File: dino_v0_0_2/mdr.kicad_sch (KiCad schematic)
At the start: 12 parts, among them U18 74LS373, U22 74LS02, U25 74LS245, U34 74LS373, U37 74LS04, U39 74LS00

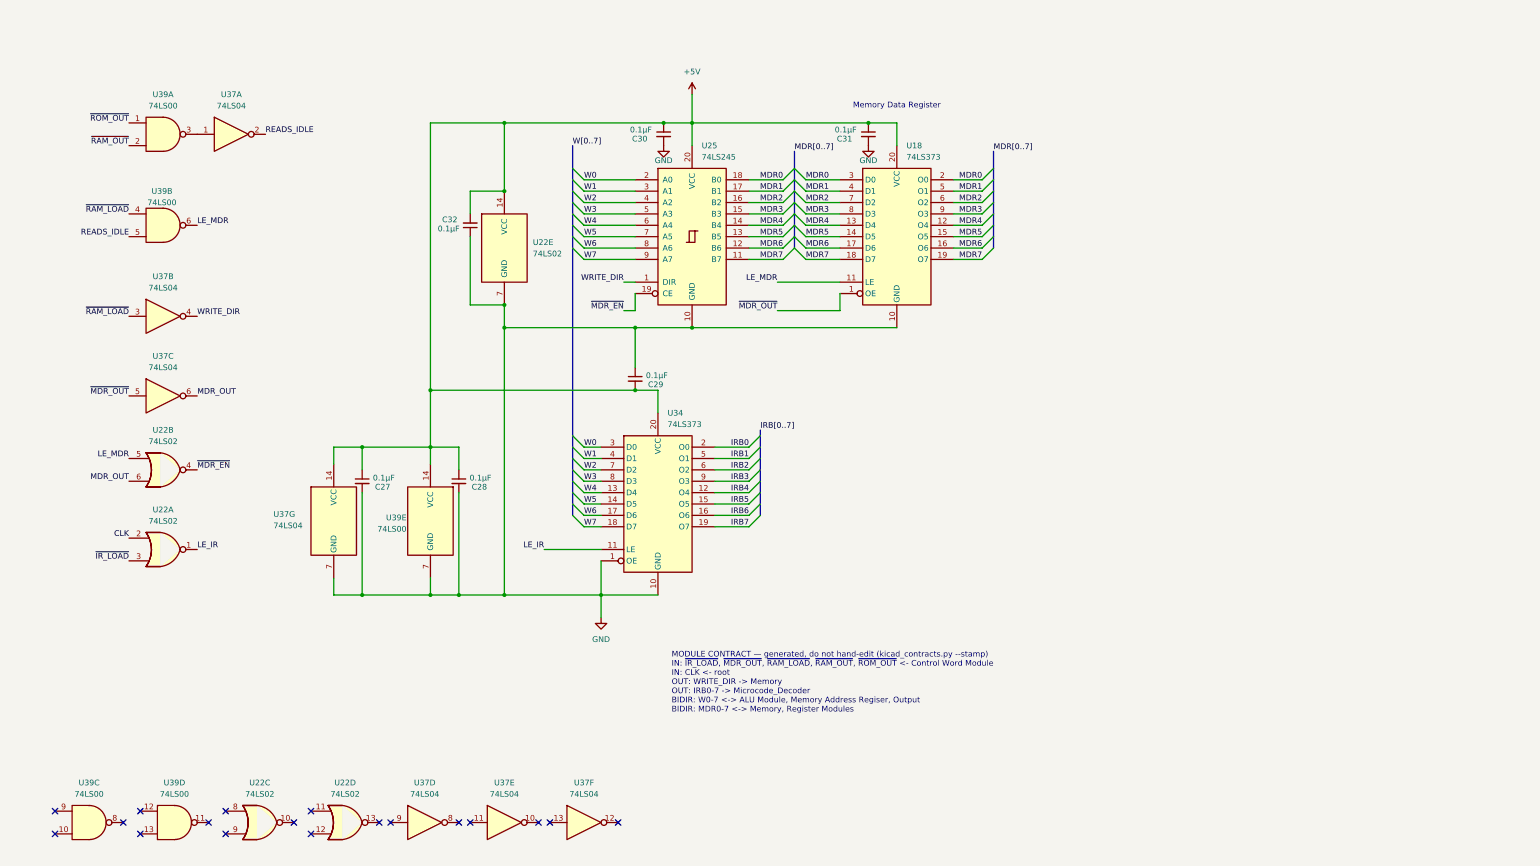
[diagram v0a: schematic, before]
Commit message: Machine Complete
All ten DINO modules bench-proven on the ATmega2560 rig: root, pc,
microcode, control_word, mdr, registers, mar, memory, alu, io. Coverage
lint reports 0 gaps and 0 pending.

Test modules (mod_*.c) plus host-tested expect models (cw/mdr/reg/mar/
mem/alu_expect.h) — pure logic, no AVR headers, exhaustive host tests
written RED before any bench run. Every assertion was netlist-verified
against the schematic before it was encoded.

Generators, so no table is hand-maintained:
  kicad_contracts.py   contracts + pinmap from the KiCad netlist
  microcode_gen.py     microcode ROM images
  progrom_gen.py       program ROM (DIAG + the milestone program)
  layout_gen.py        breadboard placement, slot maps, wiring guides

Two house rules learned the hard way and now codified in BRINGUP.md:
  mirror-witness   a write-then-read through one bus bank is
                   permutation-blind; every module needs an asymmetric
                   path (this is what caught the flipped PORTF->MDR bank)
  phantom power    rig lines feed DUT VCC through input clamp diodes, so
                   an unpowered board reads fine; every module gets a
                   power test holding outputs at the non-sourcing level

The ALU slot map in layout_gen.py is AS-BUILT and FROZEN — read off the
strip by beeping each slot to its chip pin, not derived. Once a strip is
populated its slot map is copper.

Housekeeping: .gitignore for __pycache__, KiCad .lck, Obsidian workspace
state, and compiled host-test binaries; those are untracked here.

Next: the integration ladder (INT-A/B/B2/C/D/E), then free-run of
LDAI 5; LDBI 3; ADD; OUT; HALT — the milestone, where the machine adds
two numbers.

Co-Authored-By: Claude Opus 5 (1M context) <noreply@anthropic.com>
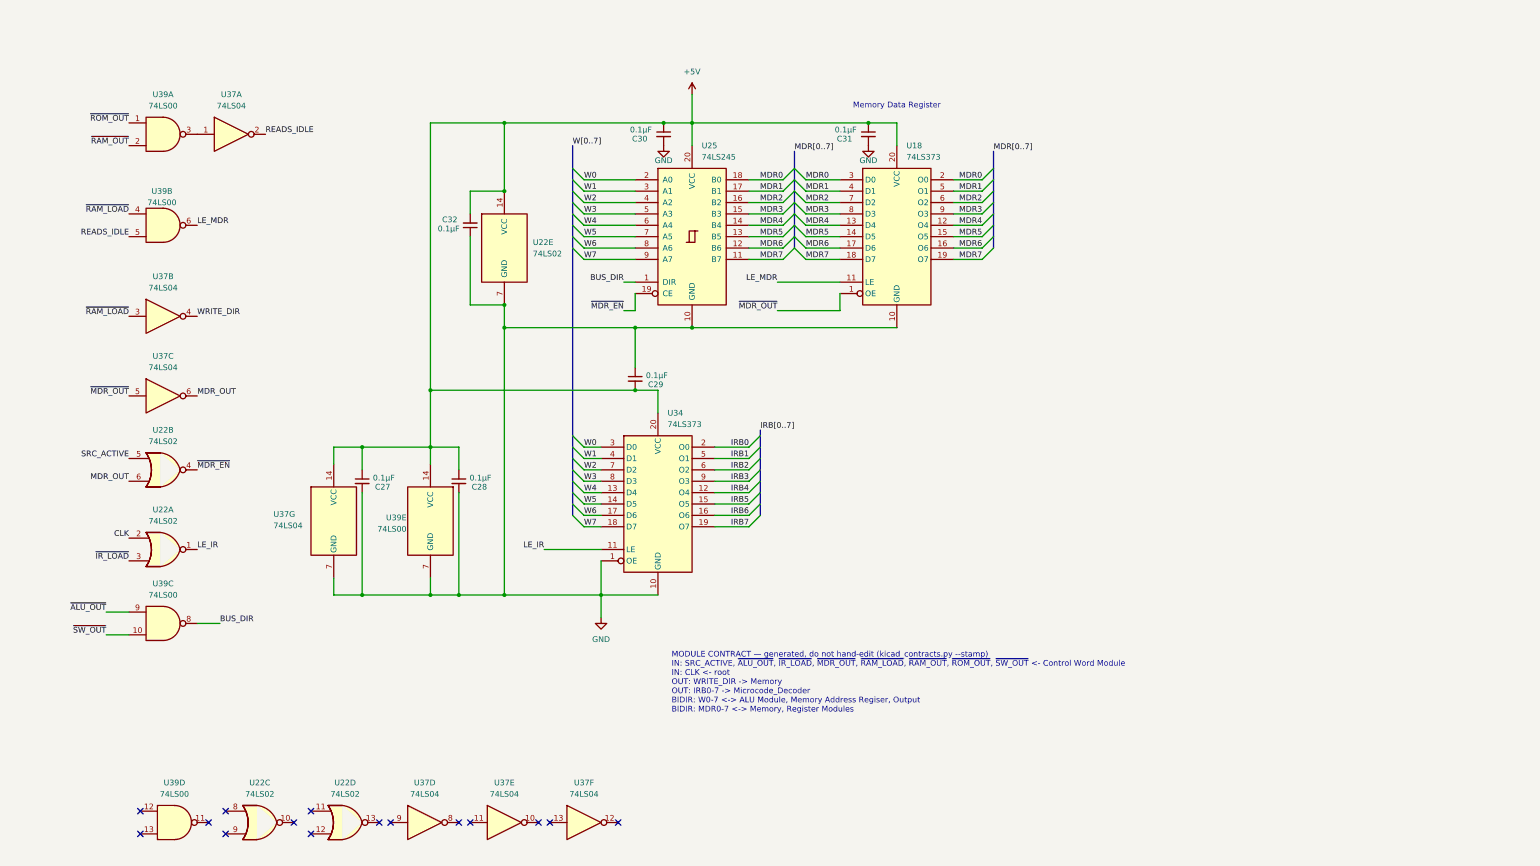
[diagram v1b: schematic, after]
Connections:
- net LE_MDR: no longer U22.5
- net WRITE_DIR: no longer U25.1 (DIR)
- net ~{SW_OUT}: now reaches U39.10
- net BUS_DIR: now reaches U39.8
- net BUS_DIR: now also U25.1 (DIR)
- net ~{ALU_OUT}: now reaches U39.9
- new net SRC_ACTIVE: U22.5
- no-connect marks 18 -> 15
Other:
- note added: "MODULE CONTRACT — generated, do not hand-edit (kicad_contracts.py --stamp) IN: SRC_ACTIVE, ~{ALU_OUT}, ~{IR_LOAD}, ~{MDR_OUT}, ~{RAM_LOAD}, ~{RAM_OUT}, ~{ROM_OUT}, ~{SW_OUT} <- Control Word Module IN: CLK <- root OUT: WRITE_DIR -> Memory OUT: IRB0-7 -> Microcode_Decoder BIDIR: W0-7 <-> ALU Module, Memory Address Regiser, Output BIDIR: MDR0-7 <-> Memory, Register Modules"
- note removed: "MODULE CONTRACT — generated, do not hand-edit (kicad_contracts.py --stamp) IN: ~{IR_LOAD}, ~{MDR_OUT}, ~{RAM_LOAD}, ~{RAM_OUT}, ~{ROM_OUT} <- Control Word Module IN: CLK <- root OUT: WRITE_DIR -> Memory OUT: IRB0-7 -> Microcode_Decoder BIDIR: W0-7 <-> ALU Module, Memory Address Regiser, Output BIDIR: MDR0-7 <-> Memory, Register Modules"
- moved on the sheet: U39C
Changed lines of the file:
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@@
 		)
 	)
-	(text "MODULE CONTRACT — generated, do not hand-edit (kicad_contracts.py --stamp)\nIN: ~{IR_LOAD}, ~{MDR_OUT}, ~{RAM_LOAD}, ~{RAM_OUT}, ~{ROM_OUT} <- Control Word Module\nIN: CLK <- root\nOUT: WRITE_DIR -> Memory\nOUT: IRB0-7 -> Microcode_Decoder\nBIDIR: W0-7 <-> ALU Module, Memory Address Regiser, Output\nBIDIR: MDR0-7 <-> Memory, Register Modules"
+	(text "MODULE CONTRACT — generated, do not hand-edit (kicad_contracts.py --stamp)\nIN: SRC_ACTIVE, ~{ALU_OUT}, ~{IR_LOAD}, ~{MDR_OUT}, ~{RAM_LOAD}, ~{RAM_OUT}, ~{ROM_OUT}, ~{SW_OUT} <- Control Word Module\nIN: CLK <- root\nOUT: WRITE_DIR -> Memory\nOUT: IRB0-7 -> Microcode_Decoder\nBIDIR: W0-7 <-> ALU Module, Memory Address Regiser, Output\nBIDIR: MDR0-7 <-> Memory, Register Modules"
 		(exclude_from_sim no)
 		(at 159.258 171.196 0)
@@
 	)
 	(no_connect
-		(at 21.59 193.04)
-	)
-	(no_connect
 		(at 78.74 198.12)
 	)
@@
 	)
 	(no_connect
-		(at 21.59 198.12)
-	)
-	(no_connect
 		(at 59.69 193.04)
 	)
@@
 	)
 	(no_connect
-		(at 36.83 195.58)
-	)
-	(no_connect
 		(at 111.76 195.58)
 	)
@@
 		)
 	)
+	(wire
+		(pts
+			(xy 38.1 153.67) (xy 33.02 153.67)
+		)
+		(stroke
+			(width 0)
+			(type default)
+		)
+	)
 	(bus
 		(pts
@@
 	(wire
 		(pts
+			(xy 38.1 148.59) (xy 33.02 148.59)
+		)
+		(stroke
+			(width 0)
+			(type default)
+		)
+	)
+	(wire
+		(pts
 			(xy 176.53 54.61) (xy 184.15 54.61)
 		)
@@
 	(wire
 		(pts
+			(xy 53.34 151.13) (xy 58.42 151.13)
+		)
+		(stroke
+			(width 0)
+			(type default)
+		)
+	)
+	(wire
+		(pts
 			(xy 163.83 39.37) (xy 163.83 44.45)
 		)
@@
 		)
 	)
+	(label "~{SW_OUT}"
+		(at 33.02 153.67 180)
+		(effects
+			(font
+				(size 1.27 1.27)
+			)
+			(justify right bottom)
+		)
+	)
 	(label "MDR0"
 		(at 189.23 52.07 0)
@@
 		)
 	)
+	(label "~{ALU_OUT}"
+		(at 33.02 148.59 180)
+		(effects
+			(font
+				(size 1.27 1.27)
+			)
+			(justify right bottom)
+		)
+	)
 	(label "MDR1"
 		(at 189.23 54.61 0)
@@
 		)
 	)
+	(label "BUS_DIR"
+		(at 58.42 151.13 0)
+		(effects
+			(font
+				(size 1.27 1.27)
+			)
+			(justify left bottom)
+		)
+	)
 	(label "MDR2"
 		(at 228.6 57.15 180)
@@
 		)
 	)
-	(label "LE_MDR"
+	(label "SRC_ACTIVE"
 		(at 38.1 114.3 180)
 		(effects
@@
 		)
 	)
-	(label "WRITE_DIR"
+	(label "BUS_DIR"
 		(at 148.59 74.93 180)
 		(effects
@@
 	(symbol
 		(lib_id "74xx:74LS00")
-		(at 29.21 195.58 0)
+		(at 45.72 151.13 0)
 		(unit 3)
 		(body_style 1)
@@
 		(fields_autoplaced yes)
 		(property "Reference" "U39"
-			(at 29.2017 186.69 0)
+			(at 45.7117 142.24 0)
 			(show_name no)
 			(do_not_autoplace no)
@@
 		)
 		(property "Value" "74LS00"
-			(at 29.2017 189.23 0)
+			(at 45.7117 144.78 0)
 			(show_name no)
 			(do_not_autoplace no)
@@
 		)
 		(property "Footprint" ""
-			(at 29.21 195.58 0)
+			(at 45.72 151.13 0)
 			(hide yes)
 			(show_name no)
@@
 		)
 		(property "Datasheet" "http://www.ti.com/lit/gpn/sn74ls00"
-			(at 29.21 195.58 0)
+			(at 45.72 151.13 0)
 			(hide yes)
 			(show_name no)
@@
 		)
 		(property "Description" "quad 2-input NAND gate"
-			(at 29.21 195.58 0)
+			(at 45.72 151.13 0)
 			(hide yes)
 			(show_name no)

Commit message: Stack pointer + third microcode EEPROM: schematic, tooling, and ISA
Twelve chips, four sheets, seven instructions. The whole stack executes on
the gate model; the rig is detached so nothing has run on real hardware.

  U23         AT28C64B   third microcode EEPROM, CW16-23     microcode
  U70 / U71   '138       SRC / DST bank-1 decoders           control_word
  U63-U66     '169       16-bit stack pointer                stack_pointer
  U67 / U68   '245       SP hi/lo readback -> MDR            stack_pointer
  U69         '08        ~{SP_CE} = AND(~SP_UP, ~SP_DOWN)    stack_pointer
  U72 / U73   '245       PC0-7 / PC8-15 -> MDR               mdr

  LXISP 0x14   CALL 0x33   RET 0x34
  PUSHA 0x61   POPA 0x62   PUSHB 0x63   POPB 0x64

THE CONTROL WORD IS 24 BITS. Every new bit is polarised so 0xFF -- an erased
AT28C64B -- is today's machine, the same reasoning that made HALT=0xFF. Only
~{SRC_BANK} and ~{DST_BANK} are wired; ~{CIN_SEL}, ~{MISC_BANK},
~{ADDR_SEL1}, FLAG_SEL0/1 and FLAG_POL are burned into all 4096 rows and
wired to nothing, so no reburn is needed when their decode arrives.

Bank switching costs zero inverters: E3 is active-high and E1 active-low, so
bank 0 hangs off E3 and bank 1 off E1 of the same bit. SRC/DST codes 8-15 are
bank 1; word() derives the bank bit FROM the code, so a caller cannot select
SP_LO and forget to switch banks.

MISC IS NOW FULL. U29's O5/O7 were the last two free codes and the stack
spends both. O0 is the NONE slot and can never be reclaimed.

Deviations from dino_hardware_growth_plan.md, corrected inline there:

  - SRC3/DST3/MISC3 -> ~{SRC_BANK}/~{DST_BANK}/~{MISC_BANK}. A '138 has three
    address pins; the new bit is an ENABLE, not a fourth.
  - COND[2:0] -> FLAG_SEL0/FLAG_SEL1/FLAG_POL. COND0 loses KiCad's alias sort
    to CW21, steals the net off the CW bus, and produces net_not_bus_member.
  - CIN is a SELECT, not a carry value: one ROM bit cannot BE the carry.
  - MISC had two free codes, not three, and SP_LOAD is a DST d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
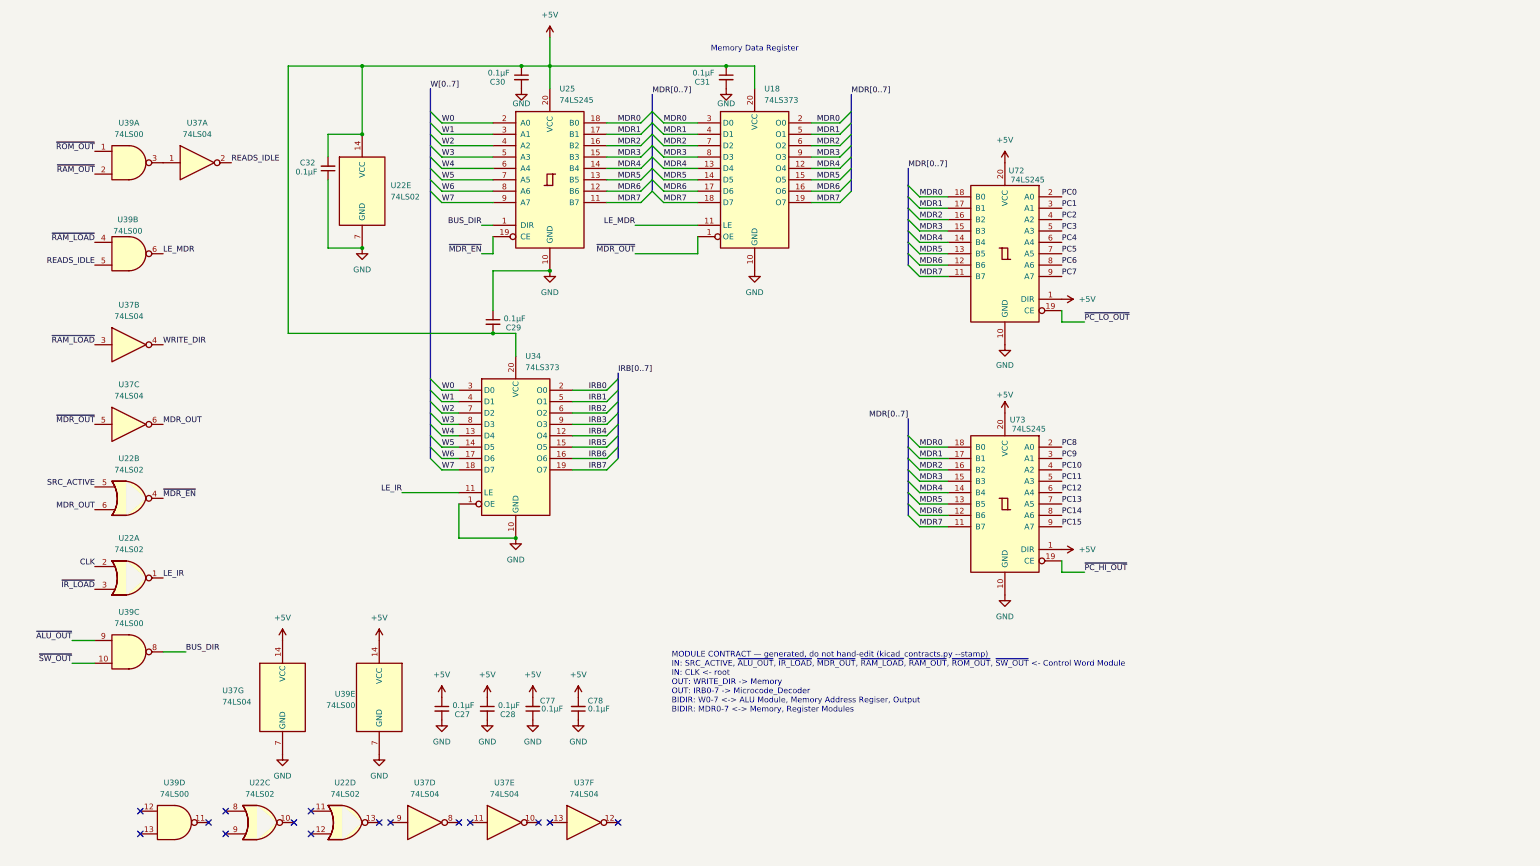
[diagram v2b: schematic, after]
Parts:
- added C77, C78: 0.1µF, symbol Device:C_Small
- added U72, U73: 74LS245, symbol 74xx:74LS245
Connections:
- net +5V: now also C77.2, C78.2, U72.1 (DIR), U72.20 (VCC), U73.1 (DIR), U73.20 (VCC)
- net GND: now also C77.1, C78.1, U72.10 (GND), U73.10 (GND)
- net MDR0: now also U72.18 (B0), U73.18 (B0)
- net MDR1: now also U72.17 (B1), U73.17 (B1)
- net MDR2: now also U72.16 (B2), U73.16 (B2)
- net MDR3: now also U72.15 (B3), U73.15 (B3)
- net MDR4: now also U72.14 (B4), U73.14 (B4)
- net MDR5: now also U72.13 (B5), U73.13 (B5)
- net MDR6: now also U72.12 (B6), U73.12 (B6)
- net MDR7: now also U72.11 (B7), U73.11 (B7)
- new net PC0: U72.2 (A0)
- new net PC1: U72.3 (A1)
- new net PC10: U73.4 (A2)
- new net PC11: U73.5 (A3)
- new net PC12: U73.6 (A4)
- new net PC13: U73.7 (A5)
- new net PC14: U73.8 (A6)
- new net PC15: U73.9 (A7)
- new net PC2: U72.4 (A2)
- new net PC3: U72.5 (A3)
- new net PC4: U72.6 (A4)
- new net PC5: U72.7 (A5)
- new net PC6: U72.8 (A6)
- new net PC7: U72.9 (A7)
- new net PC8: U73.2 (A0)
- new net PC9: U73.3 (A1)
- new net ~{PC_HI_OUT}: U73.19 (CE)
- new net ~{PC_LO_OUT}: U72.19 (CE)
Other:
- moved on the sheet: C27, C28, C29, C30, C31, C32, U18, U22A, U22B, U22E, U25, U34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
